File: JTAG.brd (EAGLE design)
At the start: 17.2 x 17 mm, 2 parts, among them U3 HIH8120

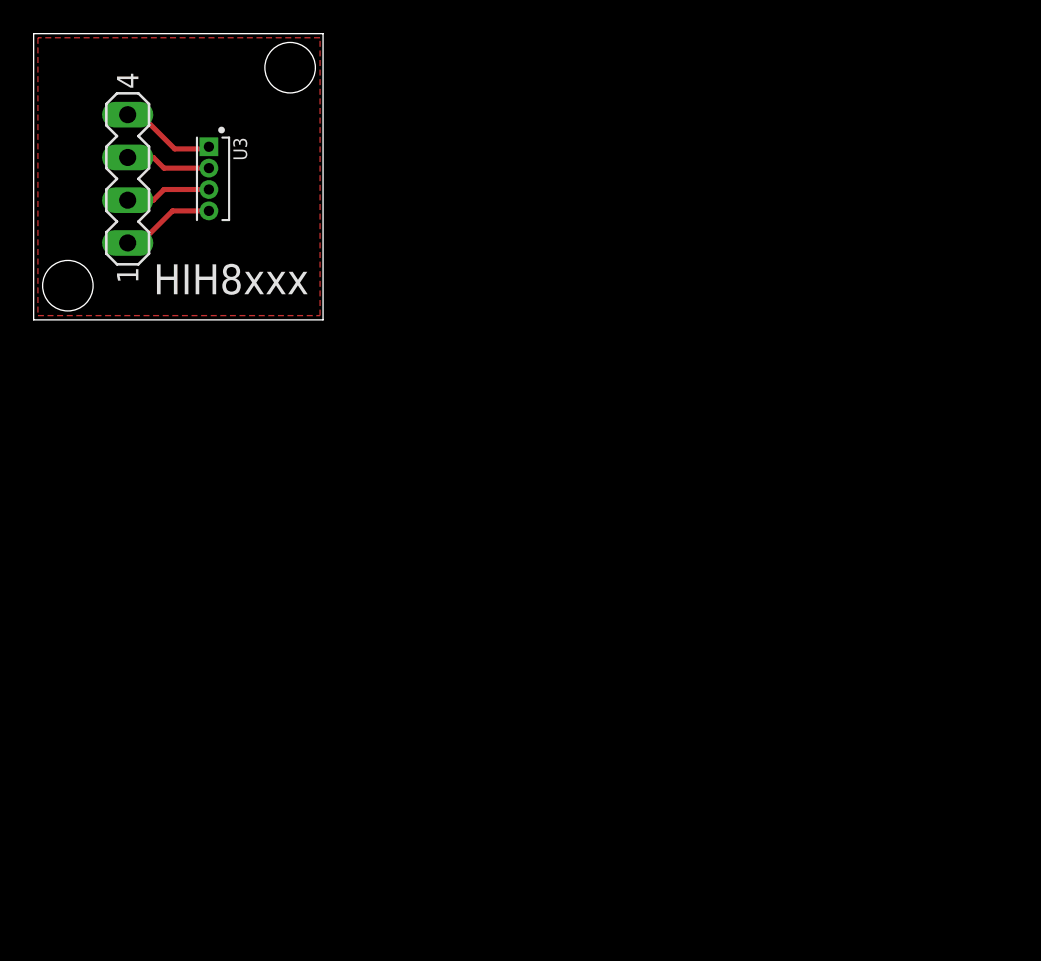
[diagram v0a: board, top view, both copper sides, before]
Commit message: added JTAG schematic and PCB  + all pictures
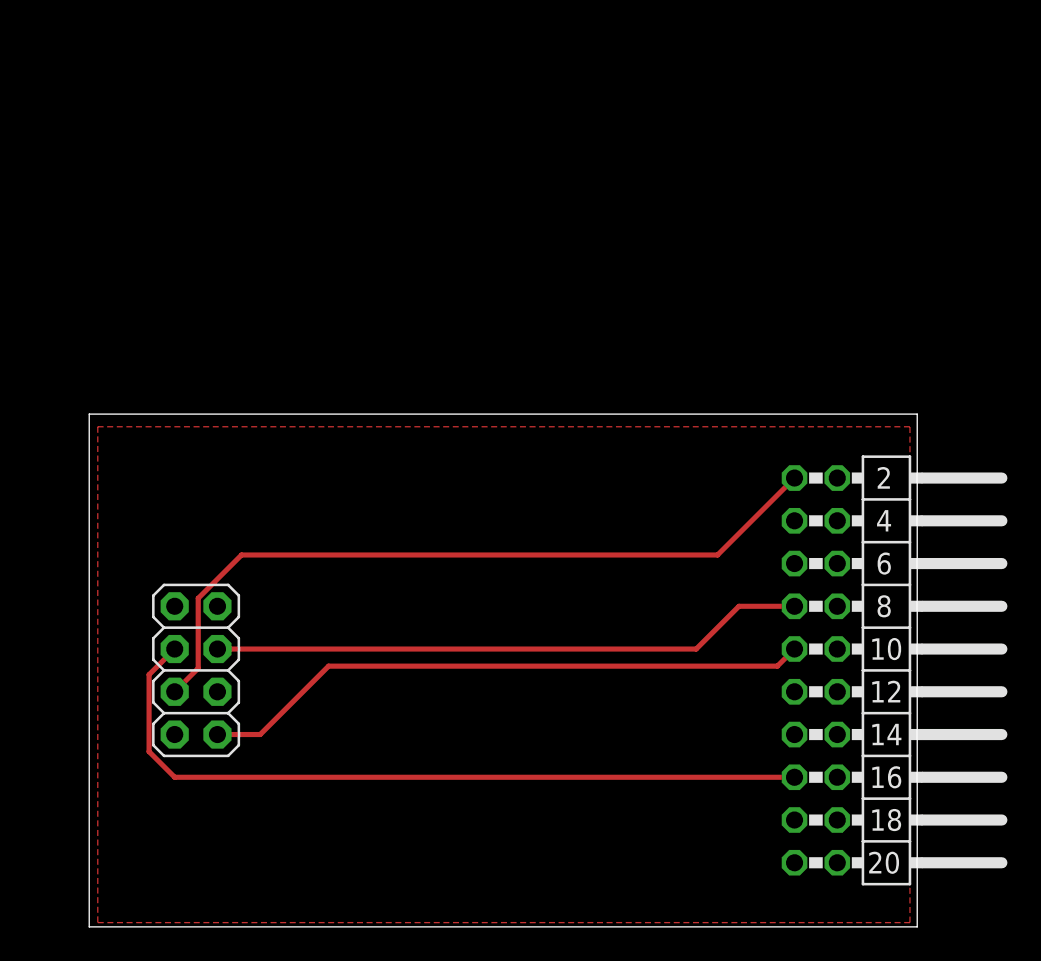
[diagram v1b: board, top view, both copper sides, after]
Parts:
- removed HIH1: T and H sensor, con-lstb:MA04-1
- removed U3: HIH8120, HIH8120-021-001:SIP191W41P127L490H390Q4
- added JP1: (no value), adafruit:2X04
- added SV2: (no value), con-lstb:MA10-2W
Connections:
- removed net N$28: HIH1.3, U3.2
- removed net N$29: HIH1.4, U3.1
- removed net N$30: HIH1.1, U3.4
- removed net N$31: HIH1.2, U3.3
- new net GND: JP1.2, SV2.10, SV2.12, SV2.14, SV2.16, SV2.18, SV2.20, SV2.4, SV2.6, SV2.8
- new net N$1: JP1.6, SV2.15
- new net N$2: JP1.4, SV2.1
- new net N$3: JP1.5, SV2.7
- new net N$4: JP1.1, SV2.9
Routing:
- net N$1: track 0.00 -> 45.7 mm
- net N$2: track 0.00 -> 44.5 mm
- net N$4: track 0.00 -> 36.4 mm
- net N$3: track 0.00 -> 35.3 mm
- net N$29: track 5.72 -> 0.00 mm
- net N$30: track 5.62 -> 0.00 mm
- net N$31: track 5.09 -> 0.00 mm
- net N$28: track 5.09 -> 0.00 mm
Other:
- board size 17.2 x 17 mm -> 49.2 x 30.5 mm
- board text removed: "HIH8xxx"
